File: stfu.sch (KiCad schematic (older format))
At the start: 92 parts, among them K1 FTDI, K2 ISP, K3 I2C, K4 SERVO, K5 V_SEL, P1 CONN_1, P2 CONN_1, P3 HAND_HI, P4 HAND_LO, P5 HAND_HI, P6 HAND_LO, P7 BATT_12V, Q1 PNP, SW1 RST, SW2 RST, SW3 SW_MODE, SW4 SW_INC, SW5 SW_DEC, SW6 SW_ENT, U1 ATMEGA328-P, U2 HEF4051B, U3 ULN2803, U4 7809, U5 7805, X1 16MHz

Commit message: Board layout, work in progress
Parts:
- removed C6: 100u, CP_5x11mm, symbol CP1
- removed D62: Z15V, DO-35_Vert, symbol DIODE_ZENER
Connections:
- net GND: now also P7.2 (PM); no longer P7.1 (P1)
- net V_BAT: now also P7.1 (P1); no longer P7.2 (PM)
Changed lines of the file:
@@
-EESchema Schematic File Version 2  date 7/10/2012 6:15:56 PM
+EESchema Schematic File Version 2  date Wednesday 11 July 2012 12:08:17 AM IST
 LIBS:stfu
 LIBS:power
@@
 Wire Wire Line
 	6750 7325 4750 7325
-Connection ~ 8375 1875
-Wire Wire Line
-	8375 1875 8375 1325
 Wire Notes Line
 	3500 625  4750 625
@@
 Connection ~ 6325 775
 Wire Wire Line
-	6325 775  6325 925
+	6325 925  6325 775
 Connection ~ 7275 1875
 Connection ~ 6775 775
@@
 	7275 1875 7275 1075
 Wire Wire Line
-	6775 925  6775 775
+	6775 775  6775 925
 Connection ~ 6525 775
 Wire Wire Line
@@
 Wire Wire Line
 	650  2150 600  2150
-Connection ~ 8575 1875
 Connection ~ 10875 6125
 Wire Wire Line
@@
 Wire Wire Line
 	8875 775  8175 775
-Connection ~ 8575 775
 Connection ~ 9875 825
 Wire Wire Line
@@
 Wire Wire Line
 	9275 1875 9275 1075
-Wire Wire Line
-	8575 775  8575 925
 Connection ~ 9675 1875
-Wire Wire Line
-	8575 1875 8575 1325
 Connection ~ 9275 1875
 Wire Wire Line
@@
 	10000 1875 10000 1775
 Connection ~ 10000 1875
-Wire Wire Line
-	8375 925  8375 775
-Connection ~ 8375 775
 Wire Wire Line
 	1250 2150 1250 2650
@@
 F 1 "BATT_12V" V 5800 1475 40  0000 C CNN
 	1    5750 1475
-	-1   0    0    1
+	-1   0    0    -1
 $EndComp
 Text Label 9675 3350 0    40   ~ 0
@@
 U 1 1 4FF2C1D0
 P 4650 5275
-F 0 "Q1" H 4575 5525 60  0000 R CNN
+F 0 "Q1" H 4650 5125 60  0000 R CNN
 F 1 "PNP" H 4650 5425 60  0000 R CNN
 	1    4650 5275
@@
 $EndComp
 $Comp
-L GND #PWR1
+L GND #PWR01
 U 1 1 4FF29B8E
 P 1050 3650
-F 0 "#PWR1" H 1050 3650 30  0001 C CNN
+F 0 "#PWR01" H 1050 3650 30  0001 C CNN
 F 1 "GND" H 1050 3580 30  0001 C CNN
 	1    1050 3650
@@
 $EndComp
 $Comp
-L GND #PWR2
+L GND #PWR02
 U 1 1 4FF29B8D
 P 1250 2650
-F 0 "#PWR2" H 1250 2650 30  0001 C CNN
+F 0 "#PWR02" H 1250 2650 30  0001 C CNN
 F 1 "GND" H 1250 2580 30  0001 C CNN
 	1    1250 2650
@@
 $EndComp
 $Comp
-L VCC #PWR3
+L VCC #PWR03
 U 1 1 4FF29B8C
 P 2350 1550
-F 0 "#PWR3" H 2350 1650 30  0001 C CNN
+F 0 "#PWR03" H 2350 1650 30  0001 C CNN
 F 1 "VCC" H 2350 1650 30  0000 C CNN
 	1    2350 1550
@@
 $EndComp
 $Comp
-L GND #PWR4
+L GND #PWR04
 U 1 1 4FF29B8B
 P 2350 5025
-F 0 "#PWR4" H 2350 5025 30  0001 C CNN
+F 0 "#PWR04" H 2350 5025 30  0001 C CNN
 F 1 "GND" H 2350 4955 30  0001 C CNN
 	1    2350 5025
@@
 $EndComp
 $Comp
-L GND #PWR5
+L GND #PWR05
 U 1 1 4FF29B88
 P 2650 2100
-F 0 "#PWR5" H 2650 2100 30  0001 C CNN
+F 0 "#PWR05" H 2650 2100 30  0001 C CNN
 F 1 "GND" H 2650 2030 30  0001 C CNN
 	1    2650 2100
@@
 $EndComp
 $Comp
-L VCC #PWR6
+L VCC #PWR06
 U 1 1 4FF29B70
 P 10800 825
-F 0 "#PWR6" H 10800 925 30  0001 C CNN
+F 0 "#PWR06" H 10800 925 30  0001 C CNN
 F 1 "VCC" H 10800 925 30  0000 C CNN
 	1    10800 825
@@
 $EndComp
 $Comp
-L GND #PWR7
+L GND #PWR07
 U 1 1 4FF29B6F
 P 10800 1825
-F 0 "#PWR7" H 10800 1825 30  0001 C CNN
+F 0 "#PWR07" H 10800 1825 30  0001 C CNN
 F 1 "GND" H 10800 1755 30  0001 C CNN
 	1    10800 1825
@@
 $EndComp
 $Comp
-L VDD #PWR9
+L VDD #PWR08
 U 1 1 4FF29B6D
 P 11000 825
-F 0 "#PWR9" H 11000 925 30  0001 C CNN
+F 0 "#PWR08" H 11000 925 30  0001 C CNN
 F 1 "VDD" H 11000 935 30  0000 C CNN
 	1    11000 825
@@
 RES
 $Comp
-L VSS #PWR10
+L VSS #PWR09
 U 1 1 4FF29B6B
 P 11000 1825
-F 0 "#PWR10" H 11000 1825 30  0001 C CNN
+F 0 "#PWR09" H 11000 1825 30  0001 C CNN
 F 1 "VSS" H 11000 1755 30  0000 C CNN
 	1    11000 1825
@@
 ISP
 $Comp
-L PWR_FLAG #FLG1
+L PWR_FLAG #FLG010
 U 1 1 4FF29B6A
 P 10000 1775
-F 0 "#FLG1" H 10000 2045 30  0001 C CNN
+F 0 "#FLG010" H 10000 2045 30  0001 C CNN
 F 1 "PWR_FLAG" H 10000 2005 30  0000 C CNN
 	1    10000 1775
@@
 	1    9675 1125
 	-1   0    0    1
-$EndComp
-$Comp
-L CP1 C6
-U 1 1 4FF29B62
-P 8575 1125
-F 0 "C6" H 8625 975 50  0000 L CNN
-F 1 "100u" H 8625 875 50  0000 L CNN
-F 2 "CP_5x11mm" H 8575 1125 60  0001 C CNN
-	1    8575 1125
-	1    0    0    -1
 $EndComp
 Text Notes 5600 600  0    60   Italic 12
@@
 MOUNTING HOLES
 $Comp
-L GND #PWR8
+L GND #PWR011
 U 1 1 4FF29B54
 P 10875 6225
-F 0 "#PWR8" H 10875 6225 30  0001 C CNN
+F 0 "#PWR011" H 10875 6225 30  0001 C CNN
 F 1 "GND" H 10875 6155 30  0001 C CNN
 	1    10875 6225
@@
 $EndComp
 $Comp
-L DIODE_ZENER D62
-U 1 1 4FF29B4B
-P 8375 1125
-F 0 "D62" V 8475 1200 40  0000 C CNN
-F 1 "Z15V" V 8275 1225 40  0000 C CNN
-F 2 "DO-35_Vert" H 8375 1125 60  0001 C CNN
-	1    8375 1125
-	0    -1   -1   0
-$EndComp
-$Comp

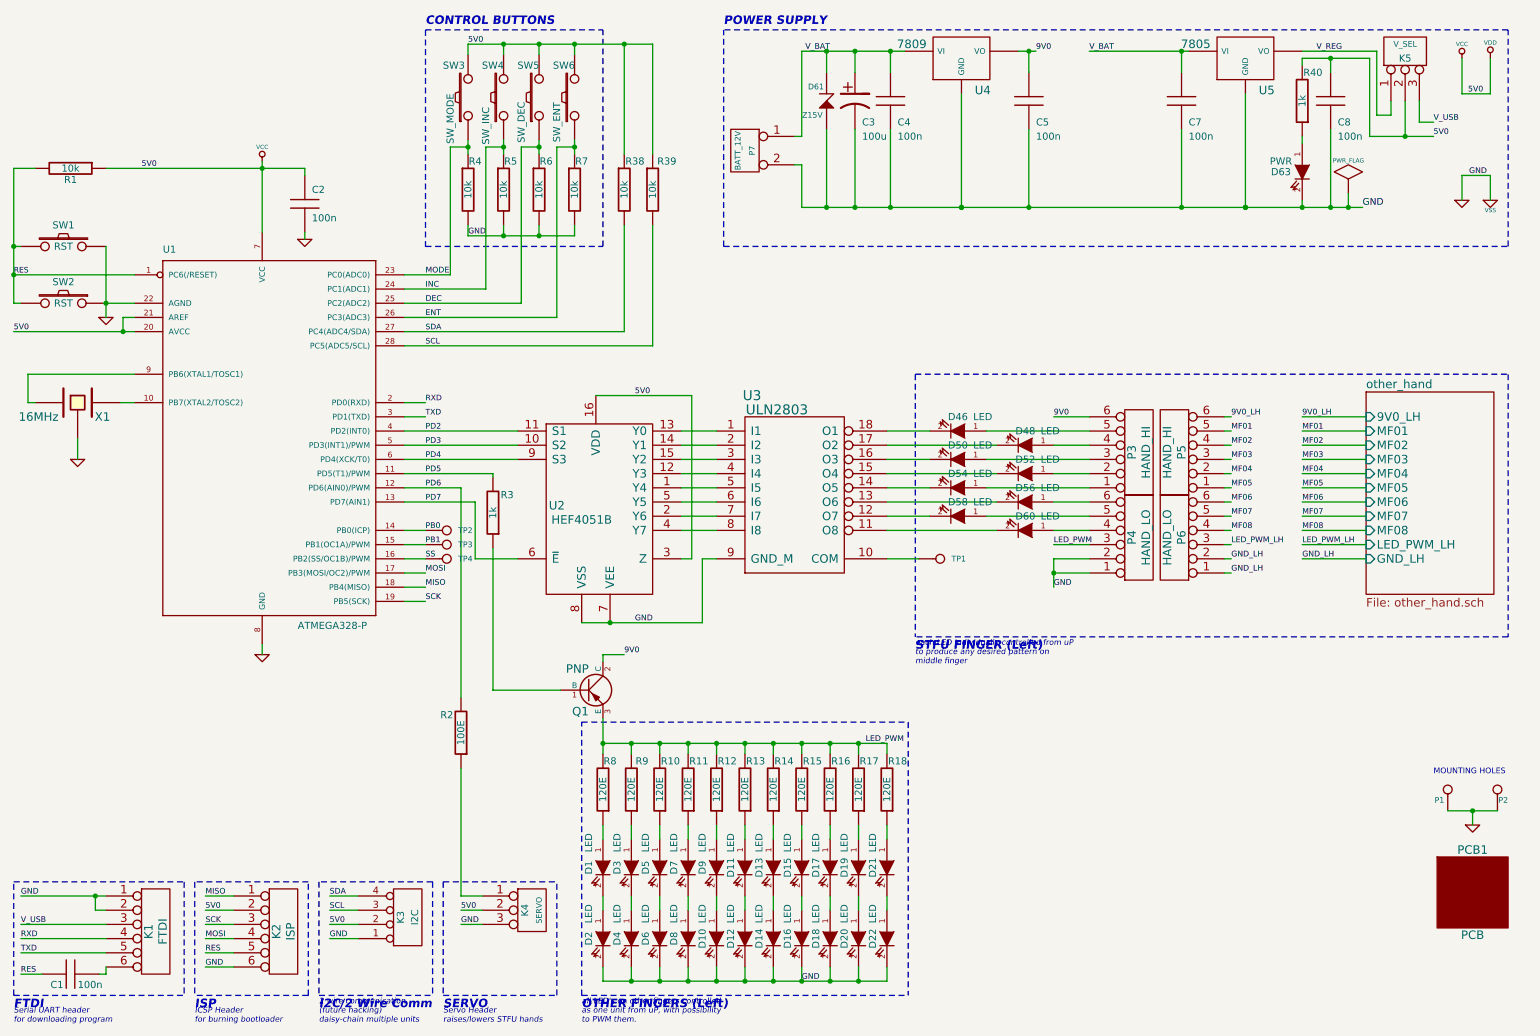
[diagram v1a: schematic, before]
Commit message: WiP, board layout progressing. Added IR receiver, removed a few buttons.
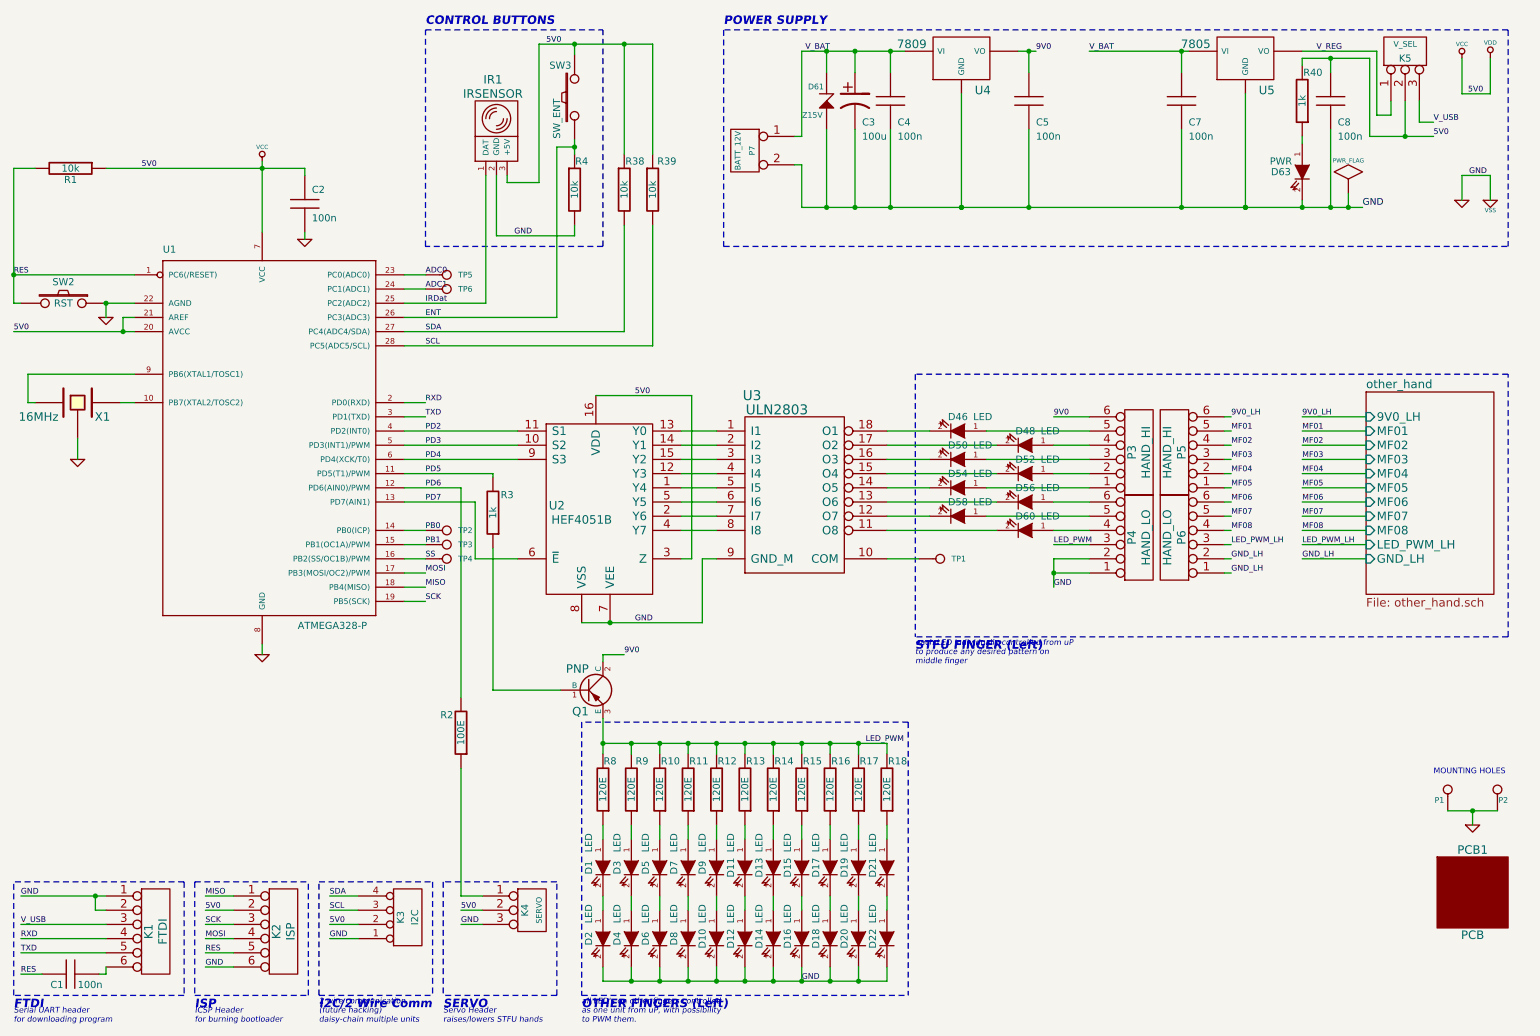
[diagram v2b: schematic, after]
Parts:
- removed R5, R6, R7: 10k, RC03, symbol R
- removed SW1: RST, SW-PB-MOD, symbol SW_PUSH
- removed SW4: SW_INC, SW_PB_V, symbol SW_PUSH
- removed SW5: SW_DEC, SW_PB_V, symbol SW_PUSH
- removed SW6: SW_ENT, SW_PB_V, symbol SW_PUSH
- added IR1: IRSENSOR, symbol IRSENSOR
- added TP5, TP6: CONN_1, symbol CONN_1
- SW3: value SW_MODE -> SW_ENT
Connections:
- net ENT: now also R4.1, SW3.1
- net GND: now also IR1.2 (GND)
- net VCC: now also IR1.3 (+5V)
- net DEC renamed IRDat
- net IRDat: now also IR1.1 (DAT)
- net INC renamed ADC1
- net ADC1: now also TP6.1
- removed net MODE: R4.1, SW3.1, U1.23 (PC0(ADC0))
- new net ADC0: TP5.1, U1.23 (PC0(ADC0))
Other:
- moved on the sheet: R4, SW3

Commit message: WiP, board layout, 185 tracks done, 49 more to go
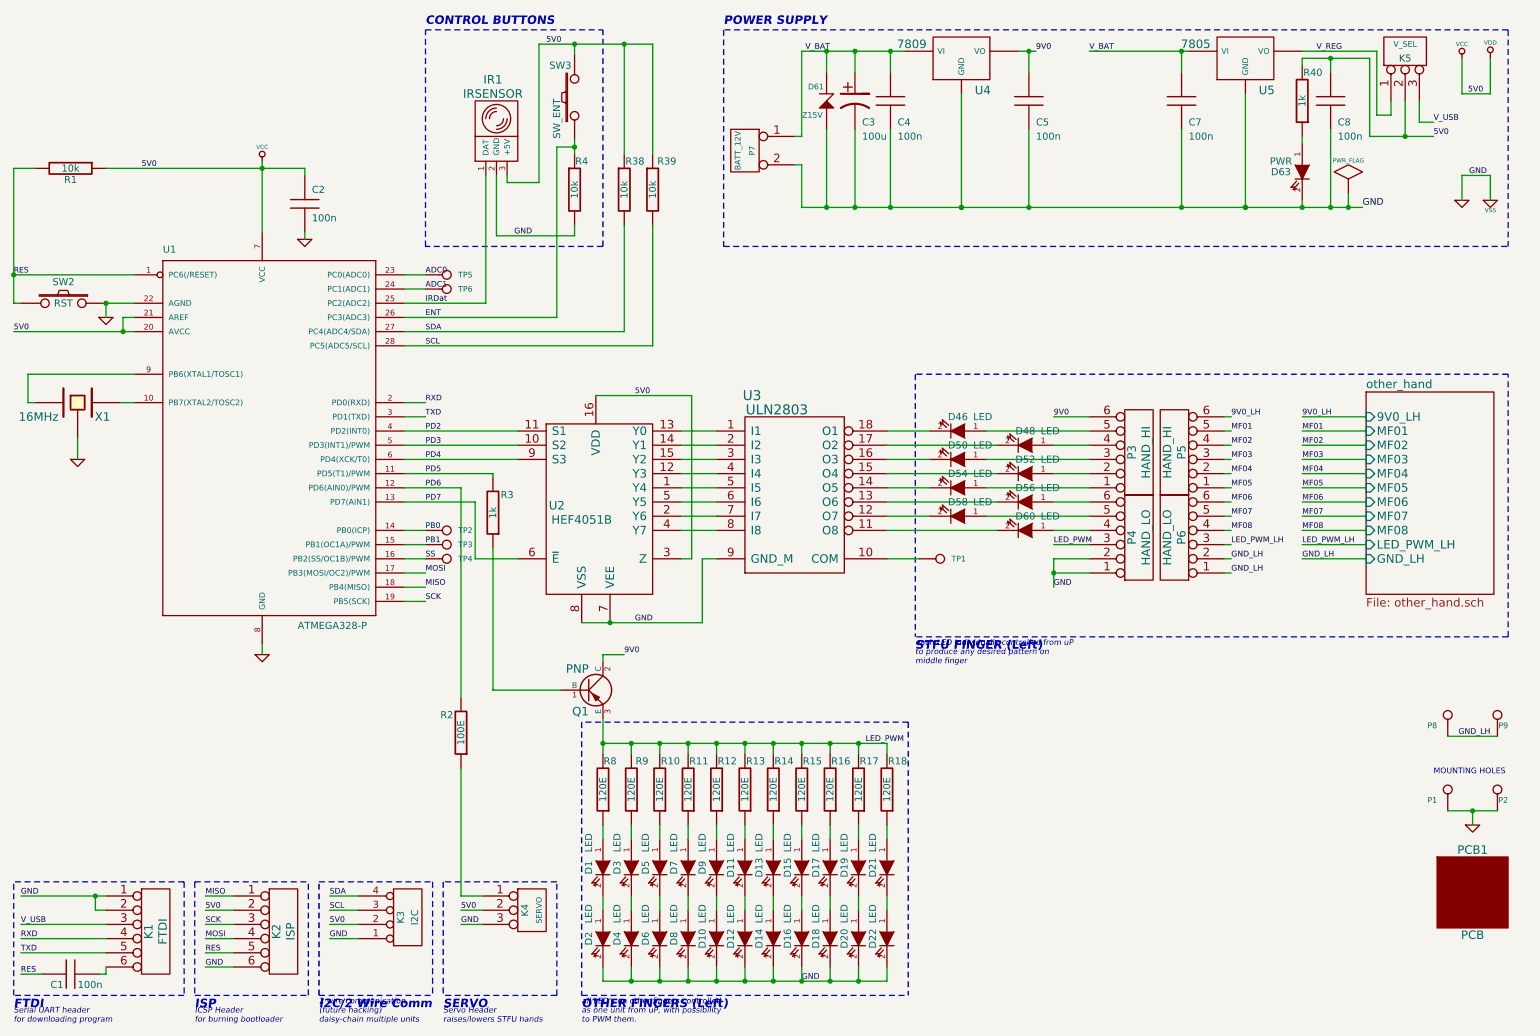
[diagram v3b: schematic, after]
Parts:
- added P8, P9: CONN_1, vite_3mm, symbol CONN_1
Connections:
- net GND_LH: now also P8.1, P9.1
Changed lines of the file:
@@
-EESchema Schematic File Version 2  date 7/12/2012 5:24:25 PM
+EESchema Schematic File Version 2  date Thursday 12 July 2012 10:52:48 PM IST
 LIBS:stfu
 LIBS:power
@@
 Comment4 ""
 $EndDescr
-Text Label 3500 2450 0    40   ~ 0
-ADC1
-Text Label 3500 2350 0    40   ~ 0
-ADC0
+Text Label 10775 5600 0    40   ~ 0
+GND_LH
 Wire Wire Line
 	3350 2450 3500 2450
@@
 	3925 2550 3925 1650
 Wire Wire Line
-	4300 1700 4300 725
+	4300 725  4300 1700
 Wire Wire Line
 	4300 1700 4075 1700
@@
 	8175 4450 7925 4450
 Wire Wire Line
-	8175 4350 7925 4350
+	7925 4350 8175 4350
 Wire Wire Line
 	7925 4150 8175 4150
@@
 	5150 7325 5150 7225
 Wire Wire Line
-	4750 7225 4750 7325
+	4750 7325 4750 7225
 Wire Wire Line
 	5950 6725 5950 6825
@@
 	4550 725  4550 800
 Wire Wire Line
-	5100 1500 5100 725
-Wire Wire Line
-	5100 725  4300 725
+	5100 725  5100 1500
+Wire Wire Line
+	4300 725  5100 725
 Connection ~ 10400 1375
 Wire Wire Line
@@
 Connection ~ 8825 775
 Wire Wire Line
-	9675 875  9675 825
+	9675 825  9675 875
 Wire Wire Line
 	9675 1375 9675 1425
@@
 Connection ~ 1175 6725
 Wire Wire Line
-	1175 6725 1175 6825
+	1175 6825 1175 6725
 Wire Wire Line
 	1175 6825 1250 6825
@@
 	1050 3650 1050 3500
 Wire Wire Line
-	2650 1650 2650 1600
+	2650 1600 2650 1650
 Connection ~ 600  2350
 Wire Wire Line
-	650  2550 600  2550
+	600  2550 650  2550
 Wire Wire Line
 	600  2550 600  1600
@@
 	3350 3250 3500 3250
 Wire Wire Line
-	2650 1600 1250 1600
+	1250 1600 2650 1600
 Wire Wire Line
 	700  3250 700  3050
@@
 	6150 7325 6150 7225
 Wire Wire Line
-	4950 7225 4950 7325
+	4950 7325 4950 7225
 Wire Wire Line
 	5350 7325 5350 7225
@@
 Connection ~ 6550 7325
 Wire Wire Line
-	6550 7325 6550 7225
+	6550 7225 6550 7325
 Wire Wire Line
 	6550 6725 6550 6825
@@
 	6350 7325 6350 7225
 Wire Wire Line
-	6750 7225 6750 7325
+	6750 7325 6750 7225
 Connection ~ 6350 7325
 Wire Wire Line
@@
 	3500 625  4750 625
 Wire Wire Line
-	6750 7325 4750 7325
+	4750 7325 6750 7325
 Wire Notes Line
 	4600 7425 6900 7425
@@
 	8175 4250 7925 4250
 Wire Wire Line
-	7925 4350 7925 4550
+	7925 4550 7925 4350
 Connection ~ 7925 4450
 Wire Wire Line
@@
 Wire Wire Line
 	3500 2350 3350 2350
+Wire Wire Line
+	10700 5600 11050 5600
+$Comp
+L CONN_1 P9
+U 1 1 4FFF0455
+P 11050 5450
+F 0 "P9" V 10975 5375 40  0000 L CNN
+F 1 "CONN_1" H 11050 5505 30  0001 C CNN
+F 2 "vite_3mm" H 11050 5450 60  0001 C CNN
+	1    11050 5450
+	0    -1   -1   0
+$EndComp
+$Comp
+L CONN_1 P8
+U 1 1 4FFF0450
+P 10700 5450
+F 0 "P8" V 10625 5525 40  0000 L CNN
+F 1 "CONN_1" H 10700 5505 30  0001 C CNN
+F 2 "vite_3mm" H 10700 5450 60  0001 C CNN
+	1    10700 5450
+	0    -1   -1   0
+$EndComp
+Text Label 3500 2450 0    40   ~ 0
+ADC1
+Text Label 3500 2350 0    40   ~ 0
+ADC0
 $Comp
 L CONN_1 TP5
@@
 U 1 1 4FF29B58
 P 10700 5975
-F 0 "P1" V 10625 6000 40  0000 L CNN
+F 0 "P1" V 10625 6050 40  0000 L CNN
 F 1 "CONN_1" H 10700 6030 30  0001 C CNN
 F 2 "vite_3mm" H 10700 5975 60  0001 C CNN
